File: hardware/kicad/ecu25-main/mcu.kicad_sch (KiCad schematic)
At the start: 29 parts, among them J11 TC2030 SWD, J14 DEBUG_UART, U12 STM32F407VGT6, Y1 8MHz, Y2 32.768kHz

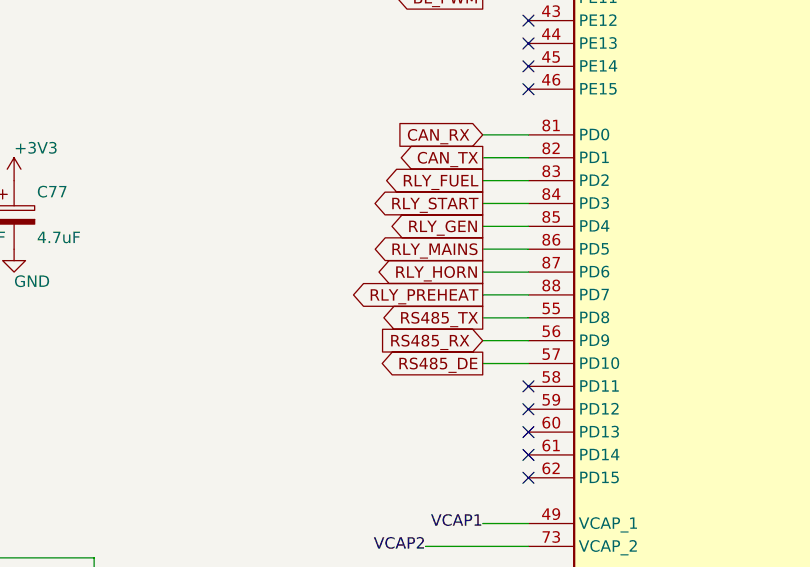
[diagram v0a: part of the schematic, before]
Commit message: Convert hardware to 12 V system; pilot-duty output stage
The target set is a Kirloskar KG4-25WS1 (engine 3R550ETA 4G1, CPCB IV+):
12 V electrical system, 75 Ah battery, 3-cylinder CRDi with EGR + DOC.
The board was designed 24 V throughout, which was wrong.

Power:
- Rails renamed +24V/+24V_SW -> +12V/+12V_SW
- Buck UVLO 8.0 V -> 6.5 V (R3 30.1k), RON 100k -> 49.9k to hold ~300 kHz
  from a 12 V input
- New D3 blocking Schottky + C9 2200uF hold-up on the buck input. UVLO now
  senses the hold-up node, not the battery: sensing the battery would trip EN
  the moment the harness sagged during crank and switch the buck off while C9
  still held charge. Sized for >50 ms down to 6.5 V with the backlight shed
- Input protection rescaled for 12 V: D1 SMCJ33CA -> SMCJ16CA (clamps ~26 V
  not 53 V), D80 -> SMBJ16CA, D2 gate zener 15 V -> 12 V, C1 63 V -> 35 V

Outputs — the board no longer sources any field current:
- J8 becomes a 6-pole body with 5 poles wired: pin 1 OUT_COM is the common
  contact supply, fed by the INSTALLER from a fused source. Relay contact COMs
  come from it, not from the board rail
- +12V_SW now feeds only the six relay coils (200 mA) and D+ (100 mA)
- START marked pilot-only: a 12 V starter solenoid pulls 20-40 A and glow
  plugs 28-60 A, against 8 A DC contacts
- K5/K6 HORN/PREHEAT -> configurable AUX1/AUX2; on a CRDi engine the ECU owns
  the cold-start aid, so a fixed preheat channel would often go unused
- Relay coils G5LE-1-DC24 -> DC12 (360 ohm / 33 mA)

Analog rescaled for 12 V:
- DIN dividers 10k/3.3k -> 5.6k/1.8k, restoring 1.6 mA contact wetting
  (10k/3.3k gives only 0.9 mA at 12 V), debounce cap 470 nF -> 1 uF
- Battery and D+ sense 100k/6.8k -> 100k/22k, so 16 V uses most of the ADC span
- D+ excitation 220R 5W -> 120R 3W for the same 100 mA at 12 V

Verified: netlist sweep clean, no courtyard overlaps, nothing outside the
outline, DRC reports no errors (unrouted ratsnest and silk warnings aside).
Docs and firmware follow in the next com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
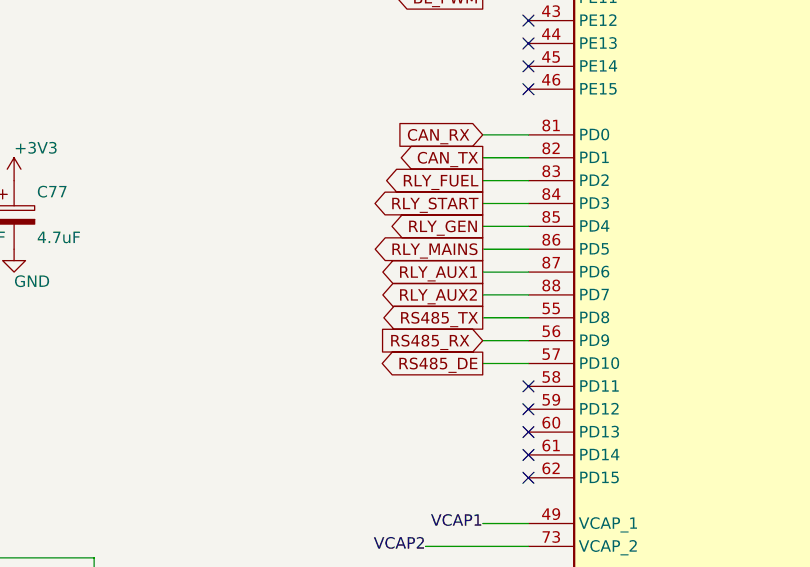
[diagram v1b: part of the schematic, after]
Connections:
- net RLY_HORN renamed RLY_AUX1
- net RLY_PREHEAT renamed RLY_AUX2
